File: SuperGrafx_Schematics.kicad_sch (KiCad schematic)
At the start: 13 parts, among them IC110 HSRM20256LM, IC111 HuC6280

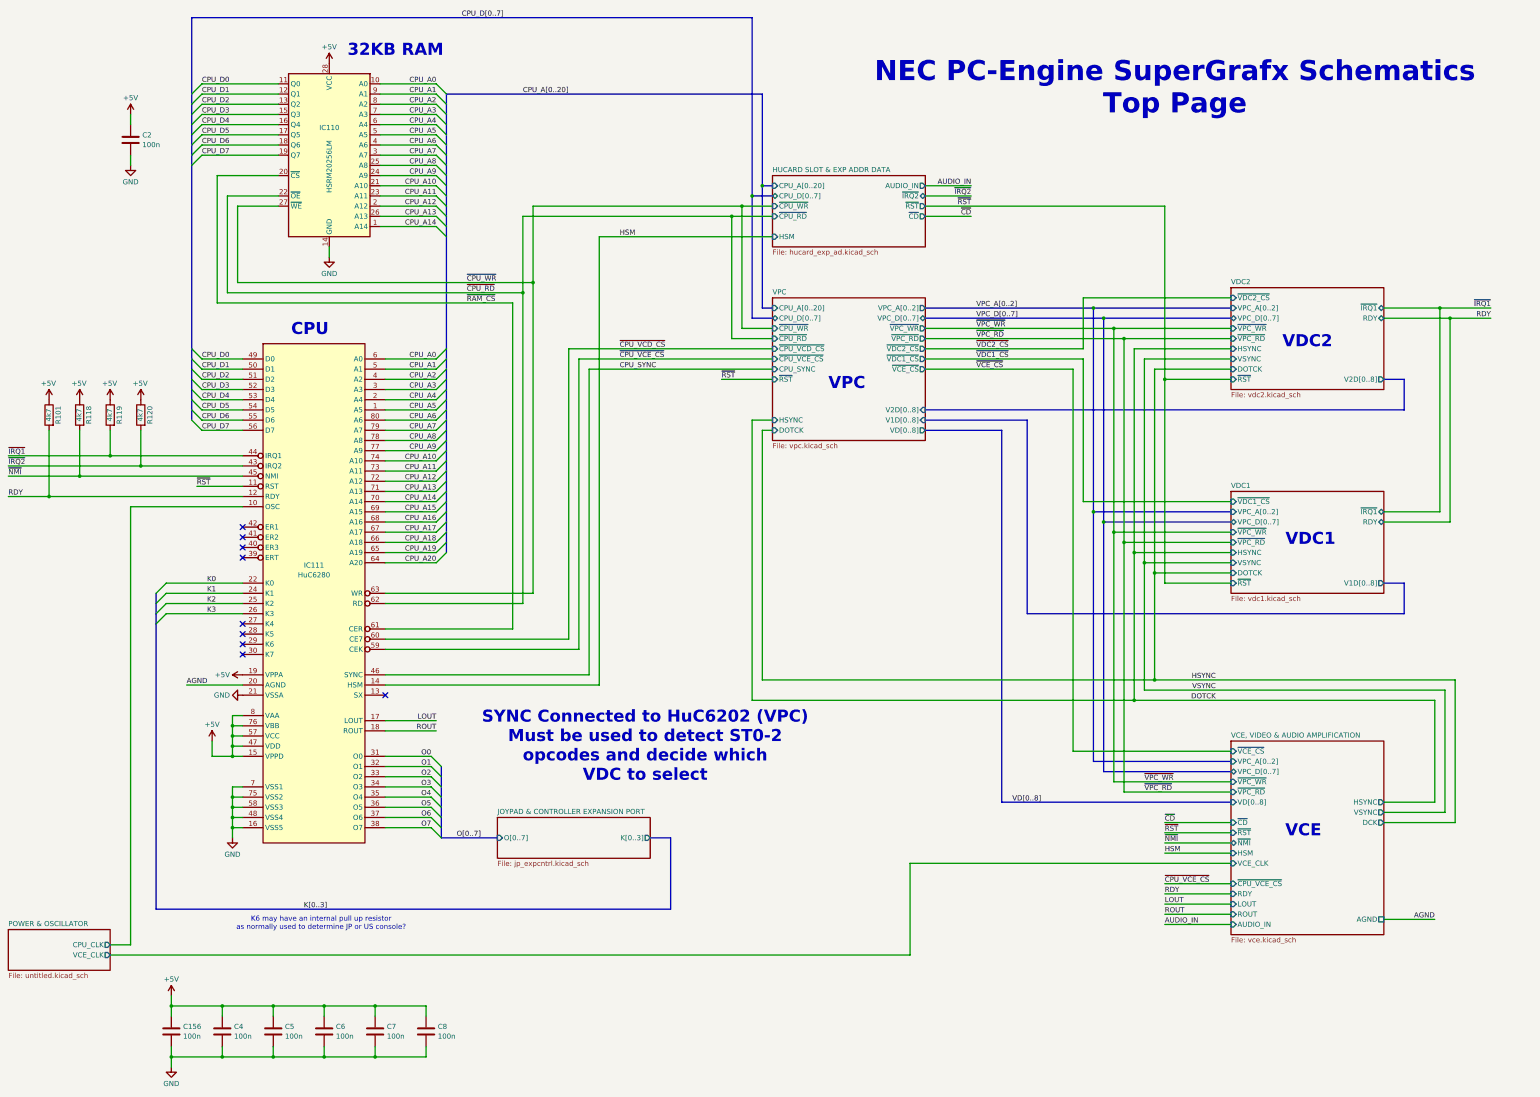
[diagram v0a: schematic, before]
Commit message: Missed out CD dection signal to main CPU and found values of decoupling capacitors under CPU hidden by EMI shield.
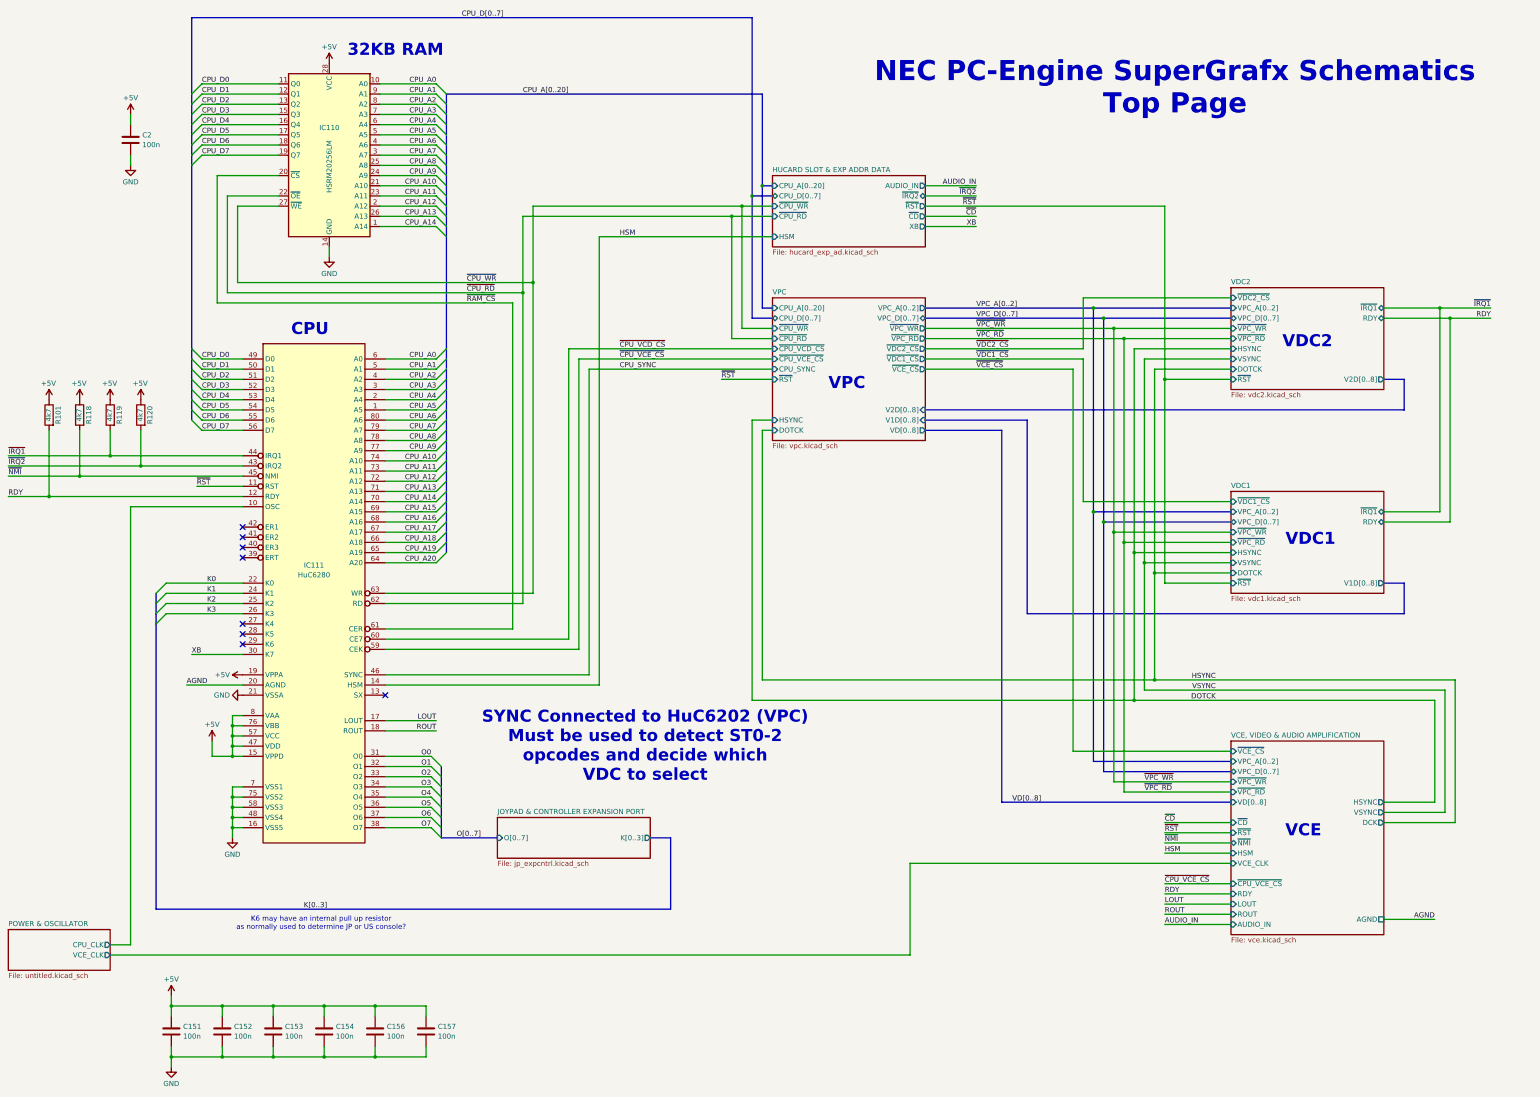
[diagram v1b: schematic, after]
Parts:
- renumbered C8 to C151, C7 to C152, C4 to C153, C5 to C154, C6 to C157
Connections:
- net XB: now reaches IC111.30 (K7)
- no-connect marks 9 -> 8
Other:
- sheet HUCARD SLOT & EXP ADDR DATA ports: added XB; removed none
- moved on the sheet: C151, C152, C153, C154, C156, C157
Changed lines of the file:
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@@
 	)
 	(no_connect
-		(at 83.82 175.26)
-	)
-	(no_connect
 		(at 83.82 167.64)
 	)
@@
 	(wire
 		(pts
-			(xy 254 58.42) (xy 265.43 58.42)
+			(xy 254 58.42) (xy 266.7 58.42)
 		)
 		(stroke
@@
 	(wire
 		(pts
-			(xy 265.43 66.04) (xy 254 66.04)
+			(xy 266.7 66.04) (xy 254 66.04)
 		)
 		(stroke
@@
 	(wire
 		(pts
+			(xy 254 68.58) (xy 266.7 68.58)
+		)
+		(stroke
+			(width 0)
+			(type default)
+		)
+	)
+	(wire
+		(pts
 			(xy 308.61 101.6) (xy 330.2 101.6)
 		)
@@
 	(wire
 		(pts
-			(xy 254 60.96) (xy 265.43 60.96)
+			(xy 254 60.96) (xy 266.7 60.96)
 		)
 		(stroke
@@
 	(wire
 		(pts
+			(xy 83.82 175.26) (xy 71.12 175.26)
+		)
+		(stroke
+			(width 0)
+			(type default)
+		)
+	)
+	(wire
+		(pts
 			(xy 311.15 181.61) (xy 213.36 181.61)
 		)
@@
 	)
 	(label "~{CD}"
-		(at 265.43 66.04 180)
+		(at 266.7 66.04 180)
 		(fields_autoplaced yes)
 		(effects
@@
 		)
 	)
+	(label "XB"
+		(at 71.12 175.26 0)
+		(fields_autoplaced yes)
+		(effects
+			(font
+				(size 1.27 1.27)
+			)
+			(justify left bottom)
+		)
+	)
 	(label "AGND"
 		(at 381 241.3 180)
@@
 	)
 	(label "AUDIO_IN"
-		(at 265.43 58.42 180)
+		(at 266.7 58.42 180)
 		(fields_autoplaced yes)
 		(effects
@@
 	)
 	(label "~{IRQ2}"
-		(at 265.43 60.96 180)
+		(at 266.7 60.96 180)
 		(fields_autoplaced yes)
 		(effects
@@
 	)
 	(label "~{RST}"
-		(at 265.43 63.5 180)
+		(at 266.7 63.5 180)
 		(fields_autoplaced yes)
 		(effects
@@
 		)
 	)
+	(label "XB"
+		(at 266.7 68.58 180)
+		(fields_autoplaced yes)
+		(effects
+			(font
+				(size 1.27 1.27)
+			)
+			(justify right bottom)
+		)
+	)
 	(label "HSM"
 		(at 313.69 224.79 0)
@@
 	(symbol
 		(lib_id "Device:C")
-		(at 78.74 269.24 0)
+		(at 91.44 269.24 0)
 		(unit 1)
 		(exclude_from_sim no)
@@
 		(dnp no)
 		(fields_autoplaced yes)
-		(property "Reference" "C4"
-			(at 81.661 268.0278 0)
+		(property "Reference" "C153"
+			(at 94.361 268.0278 0)
 			(effects
 				(font
@@
 		)
 		(property "Value" "100n"
-			(at 81.661 270.4521 0)
+			(at 94.361 270.4521 0)
 			(effects
 				(font
@@
 		)
 		(property "Footprint" ""
-			(at 79.7052 273.05 0)
+			(at 92.4052 273.05 0)
 			(effects
 				(font
@@
 		)
 		(property "Datasheet" "~"
-			(at 78.74 269.24 0)
+			(at 91.44 269.24 0)
 			(effects
 				(font
@@
 		)
 		(property "Description" "Unpolarized capacitor"
-			(at 78.74 269.24 0)
+			(at 91.44 269.24 0)
 			(effects
 				(font
@@
 			(project "SuperGrafx_Schematics"
 				(path "/c0c7a18b-b71f-4912-887a-5291f0c92de2"
-					(reference "C4")
+					(reference "C153")
 					(unit 1)
 				)
@@
 	(symbol
 		(lib_id "Device:C")
-		(at 66.04 269.24 0)
+		(at 116.84 269.24 0)
 		(unit 1)
 		(exclude_from_sim no)
@@
 		(fields_autoplaced yes)
 		(property "Reference" "C156"
-			(at 68.961 268.0278 0)
+			(at 119.761 268.0278 0)
 			(effects
 				(font
@@
 		)
 		(property "Value" "100n"
-			(at 68.961 270.4521 0)
+			(at 119.761 270.4521 0)
 			(effects
 				(font
@@
 		)
 		(property "Footprint" ""
-			(at 67.0052 273.05 0)
+			(at 117.8052 273.05 0)
 			(effects
 				(font
@@
 		)
 		(property "Datasheet" "~"
-			(at 66.04 269.24 0)
+			(at 116.84 269.24 0)
 			(effects
 				(font
@@
 		)
 		(property "Description" "Unpolarized capacitor"
-			(at 66.04 269.24 0)
+			(at 116.84 269.24 0)
 			(effects
 				(font
@@
 	(symbol
 		(lib_id "Device:C")
-		(at 104.14 269.24 0)
+		(at 129.54 269.24 0)
 		(unit 1)
 		(exclude_from_sim no)
@@
 		(dnp no)
 		(fields_autoplaced yes)
-		(property "Reference" "C6"
-			(at 107.061 268.0278 0)
+		(property "Reference" "C157"
+			(at 132.461 268.0278 0)
 			(effects
 				(font
@@
 		)
 		(property "Value" "100n"
-			(at 107.061 270.4521 0)
+			(at 132.461 270.4521 0)
 			(effects
 				(font
@@
 		)
 		(property "Footprint" ""
-			(at 105.1052 273.05 0)
+			(at 130.5052 273.05 0)
 			(effects
 				(font
@@
 		)
 		(property "Datasheet" "~"
-			(at 104.14 269.24 0)
+			(at 129.54 269.24 0)
 			(effects
 				(font
@@
 		)
 		(property "Description" "Unpolarized capacitor"
-			(at 104.14 269.24 0)
+			(at 129.54 269.24 0)
 			(effects
 				(font
@@
 			(project "SuperGrafx_Schematics"
 				(path "/c0c7a18b-b71f-4912-887a-5291f0c92de2"
-					(reference "C6")
+					(reference "C157")
 					(unit 1)
 				)
@@
 	(symbol
 		(lib_id "Device:C")
-		(at 129.54 269.24 0)
+		(at 66.04 269.24 0)
 		(unit 1)
 		(exclude_from_sim no)
@@
 		(dnp no)
 		(fields_autoplaced yes)
-		(property "Reference" "C8"
-			(at 132.461 268.0278 0)
+		(property "Reference" "C151"
+			(at 68.961 268.0278 0)
 			(effects
 				(font
@@
 		)
 		(property "Value" "100n"
-			(at 132.461 270.4521 0)
+			(at 68.961 270.4521 0)
 			(effects
 				(font
@@
 		)
 		(property "Footprint" ""
-			(at 130.5052 273.05 0)
+			(at 67.0052 273.05 0)
 			(effects
 				(font
@@
 		)
 		(property "Datasheet" "~"
-			(at 129.54 269.24 0)
+			(at 66.04 269.24 0)
 			(effects
 				(font
@@
 		)
 		(property "Description" "Unpolarized capacitor"
-			(at 129.54 269.24 0)
+			(at 66.04 269.24 0)
 			(effects
 				(font
@@
 			(project "SuperGrafx_Schematics"
 				(path "/c0c7a18b-b71f-4912-887a-5291f0c92de2"
-					(reference "C8")
+					(reference "C151")
 					(unit 1)
 				)
@@
 	(symbol
 		(lib_id "Device:C")
-		(at 91.44 269.24 0)
+		(at 104.14 269.24 0)
 		(unit 1)
 		(exclude_from_sim no)
@@
 		(dnp no)
 		(fields_autoplaced yes)
-		(property "Reference" "C5"
-			(at 94.361 268.0278 0)
+		(property "Reference" "C154"
+			(at 107.061 268.0278 0)
 			(effects
 				(font
@@
 		)
 		(property "Value" "100n"
-			(at 94.361 270.4521 0)
+			(at 107.061 270.4521 0)
 			(effects
 				(font
@@
 		)
 		(property "Footprint" ""
-			(at 92.4052 273.05 0)
+			(at 105.1052 273.05 0)
 			(effects
 				(font
@@
 		)
 		(property "Datasheet" "~"
-			(at 91.44 269.24 0)
+			(at 104.14 269.24 0)
 			(effects
 				(font
@@
 		)
 		(property "Description" "Unpolarized capacitor"
-			(at 91.44 269.24 0)
+			(at 104.14 269.24 0)
 			(effects
 				(font
@@
 			(project "SuperGrafx_Schematics"
 				(path "/c0c7a18b-b71f-4912-887a-5291f0c92de2"
-					(reference "C5")
+					(reference "C154")
 					(unit 1)
 				)
@@
 	(symbol
 		(lib_id "Device:C")
-		(at 116.84 269.24 0)
+		(at 78.74 269.24 0)
 		(unit 1)
 		(exclude_from_sim no)
@@
 		(dnp no)
 		(fields_autoplaced yes)
-		(property "Reference" "C7"
-			(at 119.761 268.0278 0)
+		(property "Reference" "C152"
+			(at 81.661 268.0278 0)
 			(effects
 				(font
@@
 		)
 		(property "Value" "100n"
-			(at 119.761 270.4521 0)
+			(at 81.661 270.4521 0)
 			(effects
 				(font
@@
 		)
 		(property "Footprint" ""
-			(at 117.8052 273.05 0)
+			(at 79.7052 273.05 0)
 			(effects
 				(font
@@
 		)
 		(property "Datasheet" "~"
-			(at 116.84 269.24 0)
+			(at 78.74 269.24 0)
 			(effects
 				(font
@@
 		)
 		(property "Description" "Unpolarized capacitor"
-			(at 116.84 269.24 0)
+			(at 78.74 269.24 0)
 			(effects
 				(font
@@
 			(project "SuperGrafx_Schematics"
 				(path "/c0c7a18b-b71f-4912-887a-5291f0c92de2"
-					(reference "C7")
+					(reference "C152")
 					(unit 1)
 				)
@@
 			(effects
 				(font
+					(size 1.27 1.27)
+				)
+				(justify right)
+			)
+		)
+		(pin "XB" output
+			(at 254 68.58 0)
+			(effects
+				(font
